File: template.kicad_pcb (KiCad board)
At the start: 2 copper layers, 95 x 65 mm, 57 parts, among them J1 power, J2 input, J3 output, J4 isp, K1 EC2-5NU, K2 EC2-5NU, K3 EC2-5NU, Q1 2N7002, Q2 2N7002, SW1 bypass switch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

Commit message: Lots of progress
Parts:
- added G***: LOGO, dsp_dev_board:frankie, F.Cu at (94.9, 91.7)
- D2, D3: footprint LED_THT:LED_D5.0mm -> LED_THT:LED_D5.0mm_compact
- moved C14 181.0 mm to (106.0, 97.0)
- moved C12 168.1 mm to (113.0, 92.2), turned to 270 degrees
- moved U6 167.3 mm to (108.2, 93.4), turned to 180 degrees
- moved C11 165.3 mm to (114.6, 95.3), turned to 90 degrees
- moved C10 156.6 mm to (117.8, 92.2), turned to 90 degrees
- moved R14 154.9 mm to (125.4, 85.3)
- moved R11 153.1 mm to (116.2, 95.3), turned to 90 degrees
- moved R8 152.9 mm to (116.2, 92.2), turned to 90 degrees
- moved R13 150.9 mm to (122.3, 85.3)
- moved D2 146.4 mm to (97.5, 113.0)
- moved C13 144.7 mm to (124.6, 87.3)
- moved J4 144.6 mm to (115.0, 69.6)
- moved R12 143.8 mm to (113.0, 95.3), turned to 270 degrees
- moved D5 143.8 mm to (120.3, 91.8), turned to 270 degrees
- moved R10 141.5 mm to (117.8, 95.3), turned to 90 degrees
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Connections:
- K2 pad 10: /preset_2_out_a -> Net-(K2-Pad10)
- K2 pad 8: /preset_2_out_b -> /preset_led
- K2 pad 9: /preset_2_in -> /5V
- K3 pad 10: Net-(K3-Pad10) -> /preset_2_out_a
- K3 pad 8: /preset_led -> /preset_2_out_b
- K3 pad 9: /5V -> /preset_2_in
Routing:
- net /effect/Vref: track 0.00 -> 39.0 mm, vias 0 -> 2
- net Net-(C8-Pad1): track 0.00 -> 23.9 mm, vias 0 -> 2
- net /effect/gain_out: track 0.00 -> 18.1 mm
- net Net-(C12-Pad2): track 0.00 -> 10.1 mm
- net Net-(R6-Pad1): track 0.00 -> 8.51 mm
- net Net-(D5-Pad1): track 0.00 -> 8.26 mm
- net /preset_led: track 0.00 -> 7.09 mm
- net 9V: track 0.00 -> 7.07 mm, vias 0 -> 1
- net Net-(D1-Pad2): track 0.00 -> 6.35 mm
- net Net-(C11-Pad1): track 0.00 -> 5.87 mm
- net Net-(C14-Pad2): track 0.00 -> 5.11 mm
- net Net-(D4-Pad2): track 0.00 -> 4.93 mm
- net Net-(D6-Pad1): track 0.00 -> 4.25 mm
- net Net-(C11-Pad2): track 0.00 -> 3.79 mm
- net Net-(R4-Pad1): track 0.00 -> 3.72 mm
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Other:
- outline, holes or cut-outs redrawn
- board text added: "bypass"
- board text added: "preset"

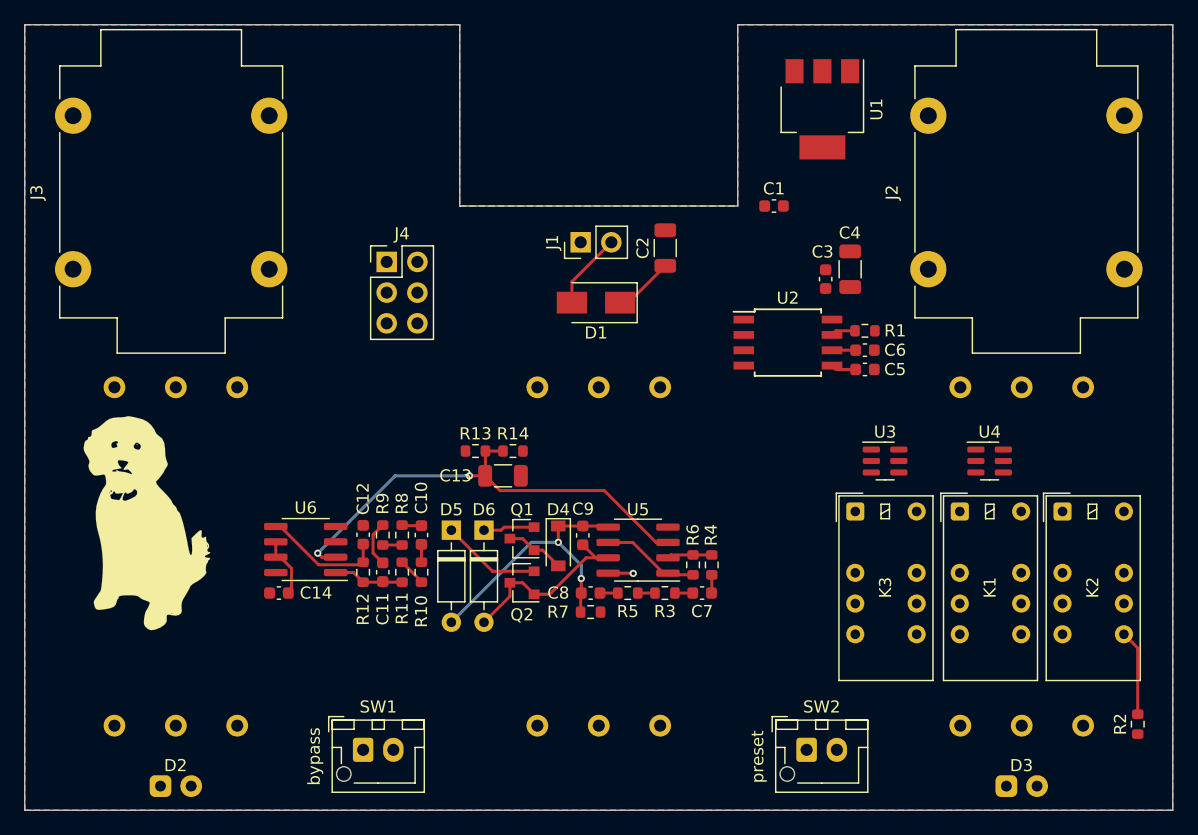
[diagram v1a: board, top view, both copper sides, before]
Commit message: Some layout improvements
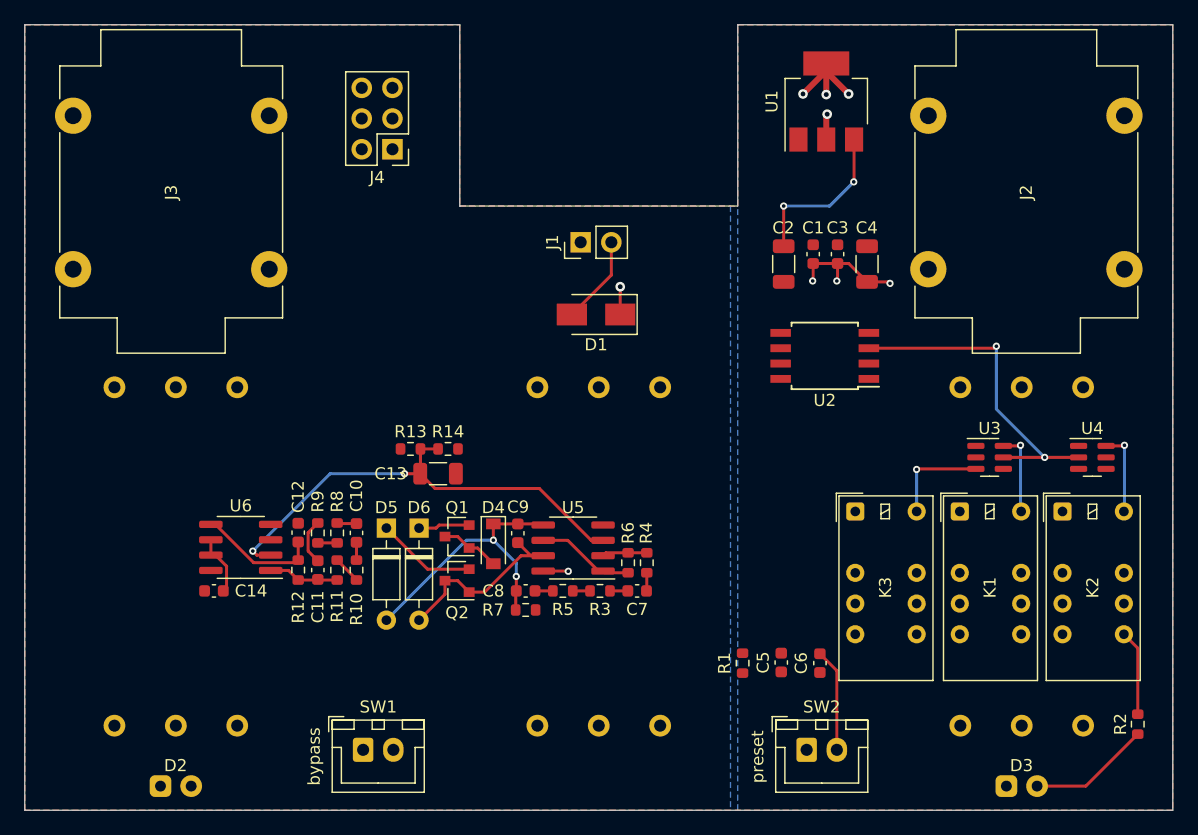
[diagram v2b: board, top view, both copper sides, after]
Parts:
- removed G***: LOGO, dsp_dev_board:frankie
- SW1, SW2: footprint Connector_JST:JST_XH_B2B-XH-AM_1x02_P2.50mm_Vertical -> Connector_JST:JST_XH_B2B-XH-A_1x02_P2.50mm_Vertical
- moved R1 29.3 mm to (144.4, 102.8), turned to 90 degrees
- moved C6 26.2 mm to (150.8, 102.8), turned to 270 degrees
- moved C5 25.2 mm to (147.6, 102.8), turned to 270 degrees
- moved C2 9.89 mm to (147.8, 69.8), turned to 270 degrees
- moved J4 9.34 mm to (115.4, 60.3), turned to 180 degrees
- moved U3 8.66 mm to (164.8, 85.8)
- moved U4 8.51 mm to (173.3, 85.8)
- moved C9 5.38 mm to (125.8, 92.1)
- moved C10 5.38 mm to (112.5, 92.0)
- moved C11 5.38 mm to (109.2, 95.1)
- moved C12 5.38 mm to (107.6, 92.0)
- moved C13 5.38 mm to (119.2, 87.2)
- moved C14 5.38 mm to (100.7, 96.8)
- moved C7 5.38 mm to (135.7, 96.8)
- moved D4 5.38 mm to (123.8, 93.0)
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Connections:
- U3 pad 3: Net-(U3-Pad3) -> /relay_3
- U3 pad 5: Net-(U3-Pad5) -> /preset_relay
- U4 pad 3: /relay_3 -> Net-(U4-Pad3)
- U4 pad 5: /preset_relay -> Net-(U4-Pad5)
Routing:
- net /preset_relay: track 0.00 -> 27.7 mm, vias 0 -> 2
- net /5V: track 0.00 -> 21.3 mm, vias 0 -> 7
- net 9V: track 7.07 -> 17.8 mm, vias 1 -> 4
- net Net-(D3-Pad2): track 0.00 -> 10.1 mm
- net /relay_3: track 0.00 -> 8.40 mm, vias 0 -> 1
- net /relay_2: track 0.00 -> 7.03 mm, vias 0 -> 1
- net /relay_1: track 0.00 -> 6.94 mm, vias 0 -> 1
- net /miso: track 1.95 -> 8.53 mm
- net /bypass_switch: track 2.08 -> 0.00 mm
- net /bypass_led: track 2.04 -> 0.00 mm
- net Net-(D1-Pad2): track 6.35 -> 7.33 mm
- added copper zone on B.Cu, net /5V

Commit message: Is this better? Tough to say
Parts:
- moved C13 25.0 mm to (143.8, 91.8)
- moved R10 24.6 mm to (136.5, 100.3)
- moved C10 24.4 mm to (136.5, 96.4)
- moved R11 22.9 mm to (133.2, 100.3)
- moved R8 22.7 mm to (133.2, 96.4)
- moved C11 21.2 mm to (129.8, 100.3)
- moved R9 21.0 mm to (129.8, 96.4)
- moved R12 19.6 mm to (126.5, 100.3)
- moved C12 19.4 mm to (126.5, 96.4)
- moved C14 18.3 mm to (118.4, 101.5), turned to 180 degrees
- moved U6 18.3 mm to (120.6, 97.6)
- moved R14 17.7 mm to (136.4, 91.6), turned to 270 degrees
- moved R13 17.4 mm to (133.1, 91.6), turned to 90 degrees
- moved R5 15.6 mm to (119.7, 84.7), turned to 270 degrees
- moved R7 13.7 mm to (126.2, 84.7), turned to 270 degrees
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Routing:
- net /effect/Vref: track 39.0 -> 17.1 mm
- net /effect/gain_out: track 18.1 -> 36.7 mm, vias 0 -> 1
- net /preset_1_out_a: track 0.00 -> 13.4 mm
- net Net-(C8-Pad1): track 23.9 -> 31.1 mm, vias 2 -> 3
- net Net-(D4-Pad2): track 4.93 -> 11.2 mm, vias 0 -> 2
- net Net-(D6-Pad1): track 4.25 -> 10.2 mm, vias 0 -> 1
- net Net-(C11-Pad1): track 5.87 -> 10.8 mm
- net Net-(R4-Pad1): track 3.72 -> 8.06 mm
- net 9V: track 17.8 -> 20.9 mm, vias 4 -> 6
- net Net-(R6-Pad1): track 8.51 -> 11.1 mm
- net /send: track 1.51 -> 3.86 mm
- net Net-(C12-Pad2): track 10.1 -> 12.4 mm
- net Net-(C8-Pad2): track 1.47 -> 3.25 mm
- net /effect/tone_pin_3: track 2.31 -> 4.03 mm
- net /preset_2_in: track 1.60 -> 3.30 mm
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
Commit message: Need to start over
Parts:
- removed J3: output, Connector_Audio:Jack_6.35mm_Neutrik_NMJ4HCD2_Horizontal
- moved J2 70.8 mm to (89.0, 70.2)
- moved SW1 0.40 mm to (113.0, 110.4)
- moved SW2 0.40 mm to (149.7, 110.4)
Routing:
- net /preset_relay: track 27.7 -> 0.00 mm, vias 2 -> 0
- net /preset_1_out_a: track 13.4 -> 0.00 mm
- net Net-(D3-Pad2): track 10.1 -> 0.00 mm
- net /miso: track 8.53 -> 0.00 mm
- net /relay_3: track 8.40 -> 0.00 mm, vias 1 -> 0
- net /preset_led: track 7.09 -> 0.00 mm
- net /relay_2: track 7.03 -> 0.00 mm, vias 1 -> 0
- net /relay_1: track 6.94 -> 0.00 mm, vias 1 -> 0

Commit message: This is better
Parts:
- added J3: output, Connector_Audio:Jack_6.35mm_Neutrik_NMJ4HCD2_Horizontal, F.Cu at (159.8, 70.2)
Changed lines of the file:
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@@
     (tracks 147)
     (zones 0)
-    (modules 56)
+    (modules 57)
     (nets 53)
   )
@@
     (add_net "Net-(U4-Pad5)")
   )
+  (module Connector_Audio:Jack_6.35mm_Neutrik_NMJ4HCD2_Horizontal (layer F.Cu)
+    (at 159.775 70.225 90)
+    (descr "M Series, 6.35mm (1/4in) mono jack, switched, with chrome ferrule and straight PCB pins, https://www.neutrik.com/en/product/nmj4hcd2")
+    (tags "neutrik jack m")
+    (fp_text reference J3 (at 6.350001 8.125 90) (layer F.SilkS)
+      (effects (font (size 1 1) (thickness 0.15)))
+    )
+    (fp_text value output (at 6.35 19 90) (layer F.Fab)
+      (effects (font (size 1 1) (thickness 0.15)))
+    )
+    (fp_text user %R (at 6.35 8.115 90) (layer F.Fab)
+      (effects (font (size 1 1) (thickness 0.15)))
+    )
+    (fp_line (start -7.33 18.23) (end 20.2 18.23) (layer F.CrtYd) (width 0.05))
+    (fp_line (start 20.2 18.23) (end 20.2 -2) (layer F.CrtYd) (width 0.05))
+    (fp_line (start 20.2 -2) (end -7.33 -2) (layer F.CrtYd) (width 0.05))
+    (fp_line (start -7.33 18.23) (end -7.33 -2) (layer F.CrtYd) (width 0.05))
+    (fp_line (start 16.82 2.295) (end 19.82 2.295) (layer F.SilkS) (width 0.12))
+    (fp_line (start 19.82 13.935) (end 19.82 2.295) (layer F.SilkS) (width 0.12))
+    (fp_line (start 16.82 13.935) (end 19.82 13.935) (layer F.SilkS) (width 0.12))
+    (fp_line (start -6.95 12.585) (end -4.03 12.585) (layer F.SilkS) (width 0.12))
+    (fp_line (start 16.82 17.335) (end 16.82 13.935) (layer F.SilkS) (width 0.12))
+    (fp_line (start 16.82 -1.105) (end 14.1 -1.105) (layer F.SilkS) (width 0.12))
+    (fp_line (start 16.82 17.335) (end 14.1 17.335) (layer F.SilkS) (width 0.12))
+    (fp_line (start -1.4 17.335) (end -4.03 17.335) (layer F.SilkS) (width 0.12))
+    (fp_line (start 11.3 17.335) (end 1.4 17.335) (layer F.SilkS) (width 0.12))
+    (fp_line (start 1.4 -1.105) (end 11.3 -1.105) (layer F.SilkS) (width 0.12))
+    (fp_line (start -4.03 -1.105) (end -1.4 -1.105) (layer F.SilkS) (width 0.12))
+    (fp_line (start -4.03 17.335) (end -4.03 12.585) (layer F.SilkS) (width 0.12))
+    (fp_line (start 16.7 17.215) (end -3.91 17.215) (layer F.Fab) (width 0.1))
+    (fp_line (start 16.7 17.215) (end 16.7 -0.985) (layer F.Fab) (width 0.1))
+    (fp_line (start 16.7 -0.985) (end -3.91 -0.985) (layer F.Fab) (width 0.1))
+    (fp_line (start -6.83 12.465) (end -6.83 3.765) (layer F.Fab) (width 0.1))
+    (fp_line (start -3.91 17.215) (end -3.91 -0.985) (layer F.Fab) (width 0.1))
+    (fp_line (start 19.7 13.815) (end 19.7 2.415) (layer F.Fab) (width 0.1))
+    (fp_line (start 19.7 13.815) (end 16.7 13.815) (layer F.Fab) (width 0.1))
+    (fp_line (start 19.7 2.415) (end 16.7 2.415) (layer F.Fab) (width 0.1))
+    (fp_line (start -6.83 12.465) (end -3.91 12.465) (layer F.Fab) (width 0.1))
+    (fp_line (start -6.83 3.765) (end -3.91 3.765) (layer F.Fab) (width 0.1))
+    (fp_line (start -6.95 12.545) (end -6.95 3.645) (layer F.SilkS) (width 0.12))
+    (fp_line (start -6.95 3.645) (end -4.03 3.645) (layer F.SilkS) (width 0.12))
+    (fp_line (start -4.03 3.645) (end -4.03 -1.105) (layer F.SilkS) (width 0.12))
+    (fp_line (start 16.82 2.295) (end 16.82 -1.105) (layer F.SilkS) (width 0.12))
+    (pad TN thru_hole circle (at 0 16.23 90) (size 3 3) (drill 1.4) (layers *.Cu *.Mask))
+    (pad SN thru_hole circle (at 12.7 16.23 90) (size 3 3) (drill 1.4) (layers *.Cu *.Mask))
+    (pad T thru_hole circle (at 0 0 90) (size 3 3) (drill 1.4) (layers *.Cu *.Mask)
+      (net 25 /out))
+    (pad S thru_hole circle (at 12.7 0 90) (size 3 3) (drill 1.4) (layers *.Cu *.Mask)
+      (net 1 GND))
+    (model ${KISYS3DMOD}/Connector_Audio.3dshapes/Jack_6.35mm_Neutrik_NMJ4HCD2_Horizontal.wrl
+      (at (xyz 0 0 0))
+      (scale (xyz 1 1 1))
+      (rotate (xyz 0 0 0))
+    )
+  )
   (module Potentiometer_THT:alpha_pot_16mm (layer B.Cu)

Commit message: Use better schematic
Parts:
- moved J4 75.9 mm to (191.0, 67.5)
- moved U3 68.4 mm to (113.9, 40.2)
- moved C3 66.9 mm to (218.2, 80.6)
- moved C4 66.9 mm to (220.6, 81.4)
- moved U1 66.9 mm to (217.2, 68.0)
- moved U2 66.9 mm to (217.1, 89.0)
- moved C1 66.9 mm to (216.2, 80.6)
- moved C2 66.9 mm to (213.7, 81.4)
- moved K1 59.5 mm to (112.2, 58.2)
- moved U4 52.3 mm to (147.9, 40.2)
- moved C13 45.4 mm to (169.3, 129.4)
- moved R13 45.4 mm to (158.6, 129.2)
- moved R14 45.4 mm to (161.9, 129.2)
- moved R5 33.6 mm to (153.3, 84.0)
- moved D4 31.1 mm to (145.8, 88.5), turned to 90 degrees
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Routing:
- net /effect/gain_out: track 36.7 -> 0.00 mm, vias 1 -> 0
- net Net-(C8-Pad1): track 31.1 -> 0.00 mm, vias 3 -> 0
- net 9V: track 20.9 -> 2.30 mm, vias 6 -> 1
- net /effect/Vref: track 17.1 -> 0.00 mm, vias 2 -> 0
- net Net-(C12-Pad2): track 12.4 -> 0.00 mm
- net Net-(D4-Pad2): track 11.2 -> 0.00 mm, vias 2 -> 0
- net Net-(R6-Pad1): track 11.1 -> 0.00 mm
- net Net-(C11-Pad1): track 10.8 -> 0.00 mm
- net Net-(D6-Pad1): track 10.2 -> 0.00 mm, vias 1 -> 0
- net Net-(R4-Pad1): track 8.06 -> 0.00 mm
- net Net-(D5-Pad1): track 6.64 -> 0.00 mm, vias 1 -> 0
- net Net-(C14-Pad2): track 6.02 -> 0.00 mm
- net Net-(C11-Pad2): track 4.66 -> 0.00 mm
- net /effect/tone_pin_3: track 4.03 -> 0.00 mm
- net /send: track 3.86 -> 0.00 mm
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- removed copper zone on B.Cu, net /5V
- removed copper zone on B.Cu, net 9V

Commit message: wooooo
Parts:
- removed Q1, Q2: 2N7002, Package_TO_SOT_SMD:SOT-23
- removed R6: 10k, Resistor_SMD:R_0603_1608Metric
- removed the U5 at (161.4, 95.6)
- R4: value 10k -> 1M
- RV5: value volume 1 (a100k) -> volume 1 (a10k)
- RV6: value volume 2 (a100k) -> volume 2 (a10k)
- moved R4 5.02 mm to (160.3, 93.8), turned to 0 degrees
- renumbered U6 to U5
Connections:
- C14 pad 2: Net-(C14-Pad2) -> Net-(C12-Pad2)
- D5 pad 1: Net-(D5-Pad1) -> /effect/gain_out
- D6 pad 1: Net-(D6-Pad1) -> Net-(D4-Pad2)
- R4 pad 1: Net-(R4-Pad1) -> /effect/Vref
- R5 pad 2: GND -> /effect/Vref
- U5 pad 2: /effect/Vref -> /effect/tone_pin_2
- U5 pad 3: /effect/tone_pin_2 -> /effect/Vref
- U5 pad 5: Net-(C12-Pad2) -> Net-(C8-Pad1)
- U5 pad 6: Net-(C14-Pad2) -> Net-(C7-Pad1)
- U5 pad 7: Net-(C14-Pad2) -> /effect/gain_out

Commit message: I think I have the positioning worked out
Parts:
- added G***: LOGO, dsp_dev_board:frankie, F.Cu at (97.5, 95.4)
- moved C4 69.4 mm to (151.8, 72.2)
- moved C3 69.4 mm to (149.4, 71.4)
- moved C1 69.4 mm to (147.4, 71.4)
- moved U1 67.4 mm to (150.8, 56.6)
- moved U2 66.0 mm to (151.5, 81.6), turned to 0 degrees
- moved C2 59.8 mm to (154.7, 72.2)
- moved J4 56.3 mm to (135.0, 73.2), turned to 270 degrees
- moved U4 47.2 mm to (162.4, 85.1)
- moved R14 42.7 mm to (132.8, 98.0)
- moved U5 42.5 mm to (135.7, 91.2), turned to 0 degrees
- moved C13 40.0 mm to (144.2, 98.4)
- moved U3 39.2 mm to (115.5, 79.5)
- moved R13 38.6 mm to (135.7, 98.0), turned to 270 degrees
- moved R4 22.1 mm to (138.7, 98.0), turned to 270 degrees
- moved C7 20.9 mm to (141.8, 90.0)
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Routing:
- net /5V: track 19.3 -> 11.3 mm, vias 6 -> 4
- net Net-(D1-Pad2): track 7.33 -> 0.00 mm
- net 9V: track 2.30 -> 0.00 mm, vias 1 -> 0
